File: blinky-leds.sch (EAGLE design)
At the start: 14 parts, among them IC1 555, IC2 4017D

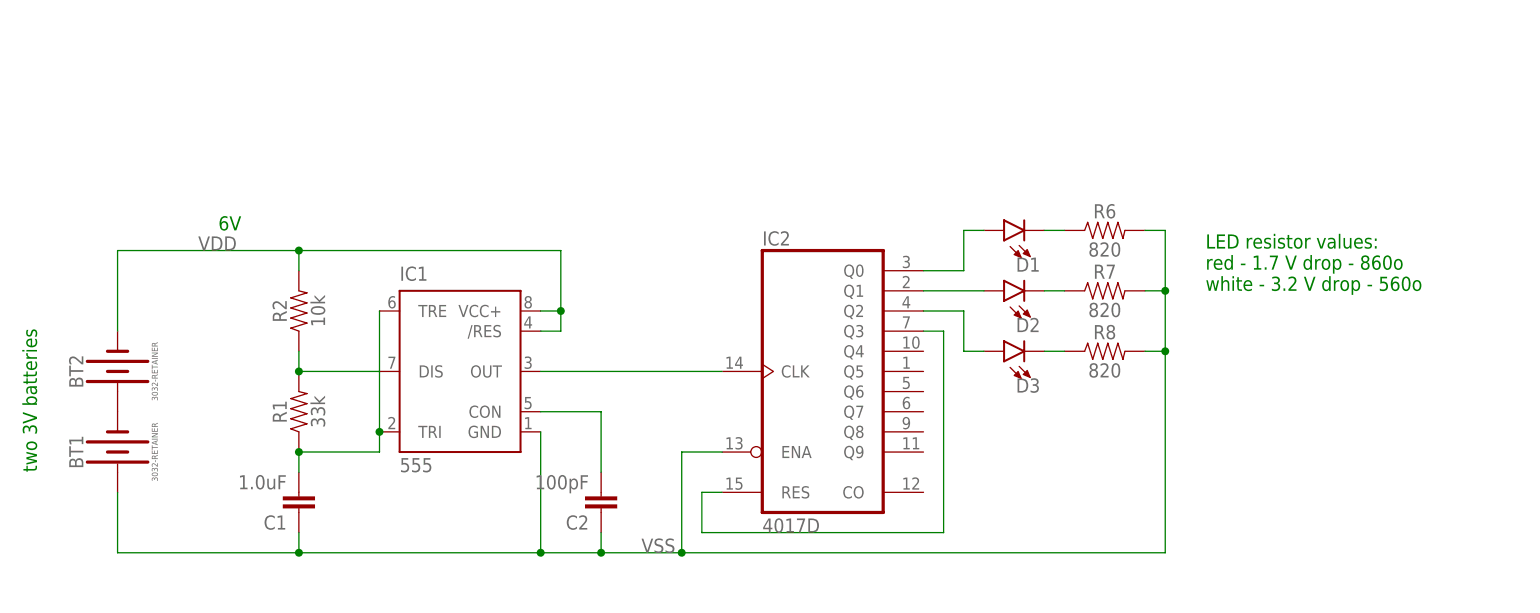
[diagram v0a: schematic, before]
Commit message: Right schematic
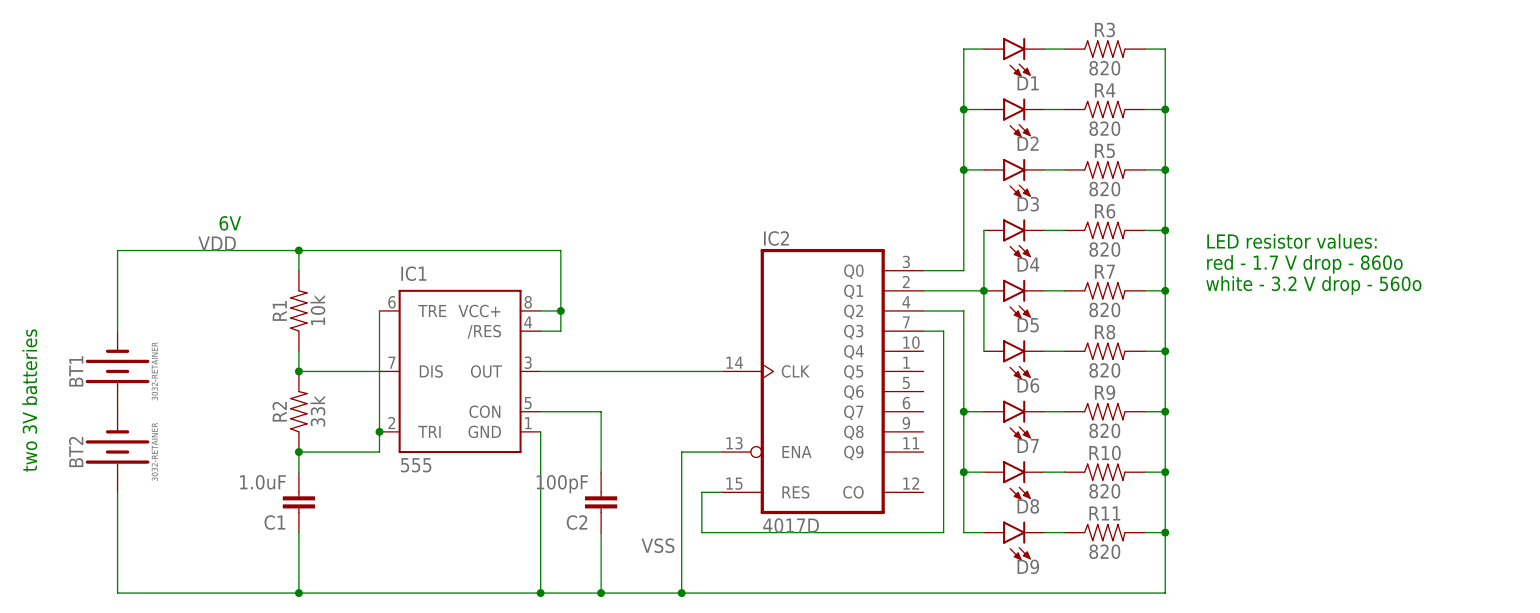
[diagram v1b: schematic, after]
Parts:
- added D4, D5, D6, D7, D8, D9: (no value), SparkFun-LED:LED0603
- added R10, R11, R3, R4, R5, R9: 820, SparkFun-Resistors:RESISTOR0603
- R1: value 33k -> 10k; device SparkFun-Resistors:33KOHM-0603-1/10W-1% -> SparkFun-Resistors:10KOHM-0603-1/10W-1%
- R2: value 10k -> 33k; device SparkFun-Resistors:10KOHM-0603-1/10W-1% -> SparkFun-Resistors:33KOHM-0603-1/10W-1%
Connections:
- removed net N$5: D3.A, IC2A.Q2
- new net N$13: D3.C, R5.1
- new net N$14: D2.C, R4.1
- new net N$15: D1.C, R3.1
- new net N$16: D9.C, R11.1
- new net N$17: D8.C, R10.1
- new net N$18: D7.C, R9.1
- new net N$20: D7.A, D8.A, D9.A, IC2A.Q2
- net N$1: now also BT1.+, BT2.-; no longer BT1.-, BT2.+
- net N$11: now also D5.C; no longer D2.C
- net N$12: now also D4.C; no longer D1.C
- net N$2: now also D6.C; no longer D3.C
- net N$3: now also D2.A, D3.A
- net N$4: now also D4.A, D5.A, D6.A; no longer D2.A
- net N$8: now also R1.1, R2.2; no longer R1.2, R2.1
- net N$9: now also R2.1; no longer R1.1
- net VDD: now also BT1.-, R1.2; no longer BT2.-, R2.2
- net VSS: now also BT2.+, R10.2, R11.2, R3.2, R4.2, R5.2, R9.2; no longer BT1.+
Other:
- moved on the sheet: BT1, BT2, D1, D2, D3, R1, R2
